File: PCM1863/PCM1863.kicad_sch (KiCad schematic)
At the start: 34 parts, among them IC1 SN74AUC1G126DCKR, IC2 NCP163ASN330T1G, IC3 NCP163ASN330T1G, J1 Conn_01x10_Male, J2 Conn_01x10_Male, J3 Conn_01x10_Male, U1 PCM1863, Y1 ASE-24.000MHZ-ET, Y2 ASE-22.000MHZ-ET

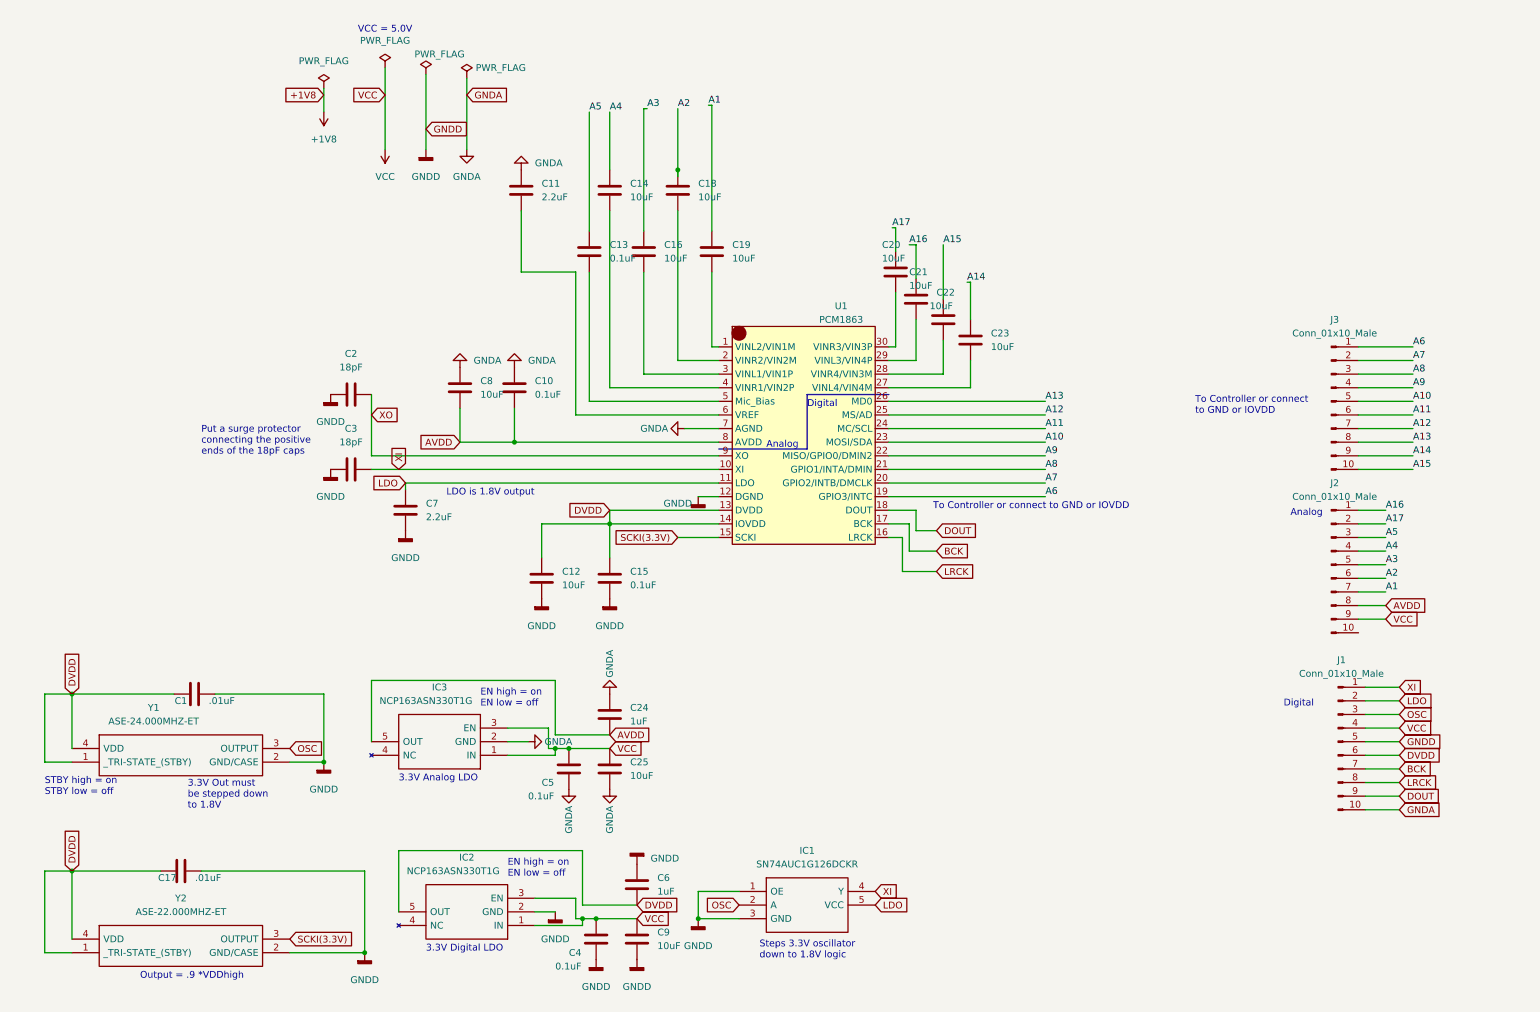
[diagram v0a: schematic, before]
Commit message: 1863 power added and schematic updated
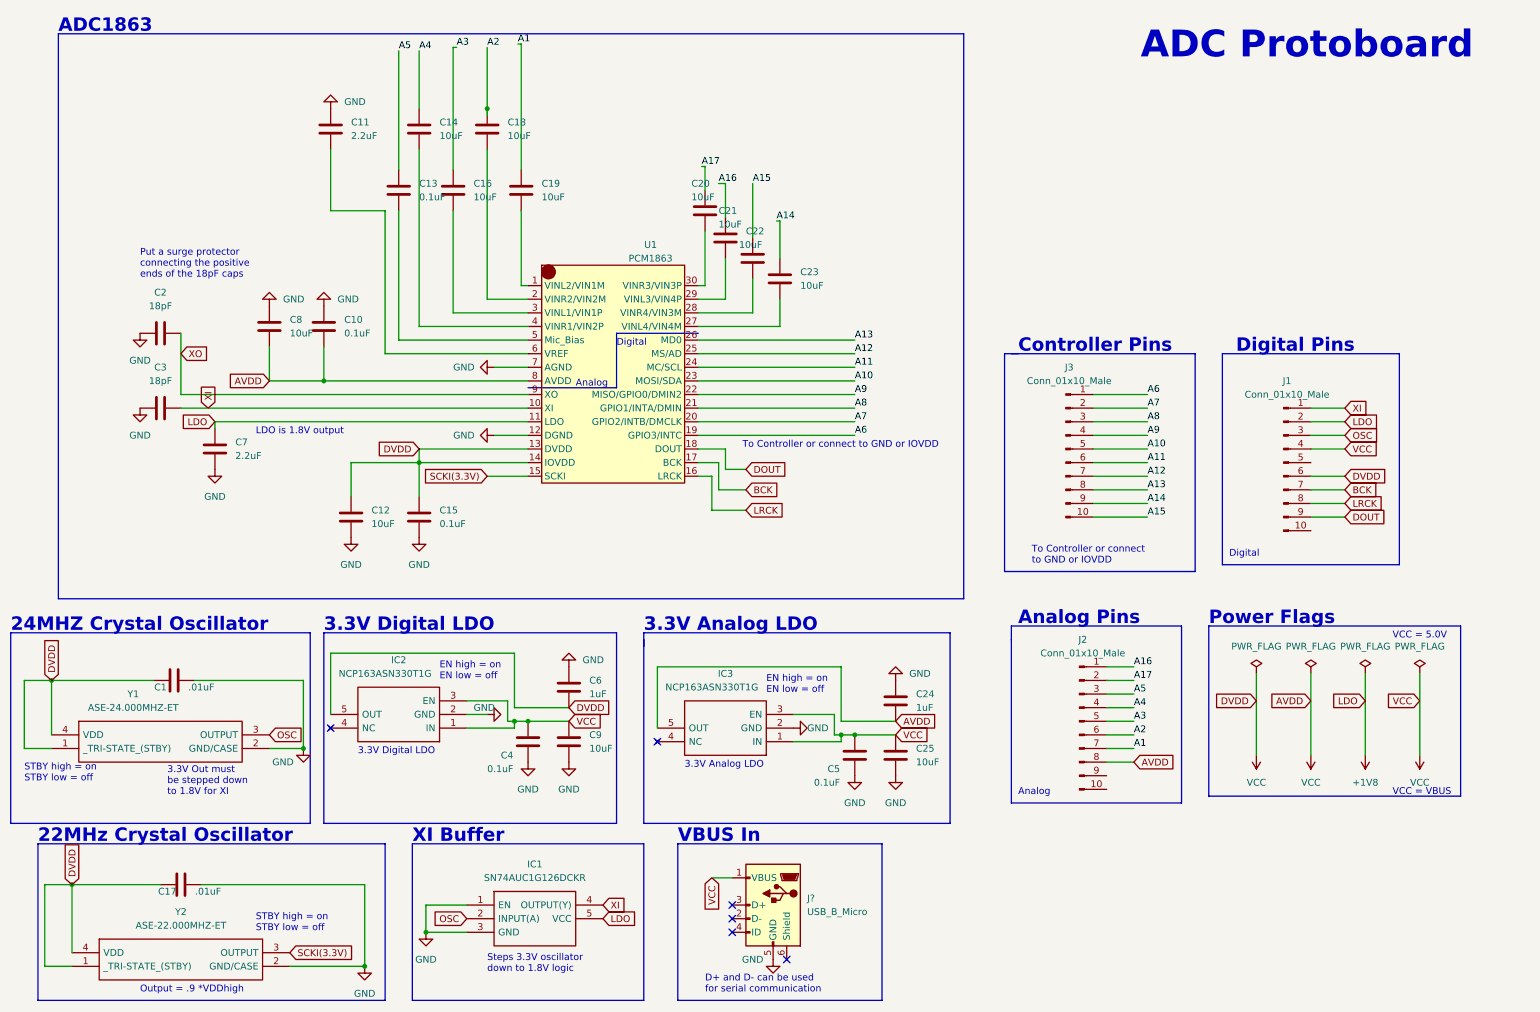
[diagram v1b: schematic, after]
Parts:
- added J?: USB_B_Micro, Connector_USB:USB_Micro-B_Wuerth_629105150521, symbol Connector:USB_B_Micro
- IC1: footprint custom_lib:SOT65P210X110-5N -> SOT65P210X110-5N
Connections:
- net AVDD is gone; now on net VCC: C10.2, C24.2, C8.2, IC3.5 (OUT), J2.8 (Pin_8), U1.8 (AVDD)
- net DVDD is gone; now on net VCC: C1.1, C12.1, C15.1, C17.1, C6.2, IC2.5 (OUT), J1.6 (Pin_6), U1.13 (DVDD), U1.14 (IOVDD), Y1.1 (_TRI-STATE_(STBY)), Y1.4 (VDD), Y2.1 (_TRI-STATE_(STBY)), Y2.4 (VDD)
- net LDO is gone; now on net +1V8: C7.1, IC1.5 (VCC), J1.2 (Pin_2), U1.11 (LDO)
- net VCC: now also J?.1 (VBUS); no longer J2.9 (Pin_9)
- net GNDA renamed GND
- net GND: now also C1.2, C12.2, C15.2, C17.2, C2.1, C3.1, C4.2, C6.1, C7.2, C9.2, IC1.1 (EN), IC1.3 (GND), IC2.2 (GND), U1.12 (DGND), Y1.2 (GND/CASE), Y2.2 (GND/CASE), J?.5 (GND); no longer J1.10 (Pin_10)
- removed net GNDD: C1.2, C12.2, C15.2, C17.2, C2.1, C3.1, C4.2, C6.1, C7.2, C9.2, IC1.1 (OE), IC1.3 (GND), IC2.2 (GND), J1.5 (Pin_5), U1.12 (DGND), Y1.2 (GND/CASE), Y2.2 (GND/CASE)
- no-connect marks 0 -> 6
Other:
- note added: "22MHz Crystal Oscillator"
- note added: "24MHZ Crystal Oscillator"
- note added: "3.3V Out must be stepped down to 1.8V for XI"
- note added: "ADC Protoboard"
- note added: "ADC1863"
- note added: "Analog Pins"
- note added: "Controller Pins"
- note added: "D+ and D- can be used for serial communication"
- note added: "Digital Pins"
- note added: "Power Flags"
- note added: "VBUS In"
- note added: "VCC = VBUS"
- note added: "XI Buffer"
- note removed: "3.3V Out must be stepped down to 1.8V"
- company: (none) -> Chameleon Engine 2023
- title: (none) -> ADC Protoboard
- moved on the sheet: C1, C10, C11, C12, C13, C14, C15, C16, C17, C18, C19, C2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

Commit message: PCB placement no trace
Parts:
- added D1, D2, D3: RED1.8, LED_SMD:LED_0603_1608Metric_Pad1.05x0.95mm_HandSolder, symbol Device:LED
- added R1, R2, R3: 2.2k, Resistor_SMD:R_0603_1608Metric_Pad0.98x0.95mm_HandSolder, symbol Device:R
- IC1: footprint SOT65P210X110-5N -> custom_lib:SOT65P210X110-5N
- gave numbers to parts that had none: 1
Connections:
- net +1V8: now also D1.2 (A)
- net GND: now also R1.2, R2.2, R3.2
- net VCC: no longer C1.1, C10.2, C12.1, C15.1, C17.1, C24.2, C6.2, C8.2, IC2.5 (OUT), IC3.5 (OUT), J1.6 (Pin_6), J2.8 (Pin_8), U1.13 (DVDD), U1.14 (IOVDD), U1.8 (AVDD), Y1.1 (_TRI-STATE_(STBY)), Y1.4 (VDD), Y2.1 (_TRI-STATE_(STBY)), Y2.4 (VDD)
- new net: D3.1 (K), R3.1
- new net: D1.1 (K), R1.1
- new net: D2.1 (K), R2.1
- new net +3.3VA: C10.2, C24.2, C8.2, D3.2 (A), IC3.5 (OUT), J2.8 (Pin_8), U1.8 (AVDD)
- new net +3V3: C1.1, C12.1, C15.1, C17.1, C6.2, D2.2 (A), IC2.5 (OUT), J1.6 (Pin_6), U1.13 (DVDD), U1.14 (IOVDD), Y1.1 (_TRI-STATE_(STBY)), Y1.4 (VDD), Y2.1 (_TRI-STATE_(STBY)), Y2.4 (VDD)

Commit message: adc v3 complete
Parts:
- added D4: RED1.8, LED_SMD:LED_0603_1608Metric_Pad1.05x0.95mm_HandSolder, symbol Device:LED
- added H1, H2, H3, H4: MountingHole_Pad, MountingHole:MountingHole_2.2mm_M2_Pad, symbol Mechanical:MountingHole_Pad
- added R4: 2.2k, Resistor_SMD:R_0603_1608Metric_Pad0.98x0.95mm_HandSolder, symbol Device:R
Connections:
- net +1V8: now also J1.5 (Pin_5); no longer J1.2 (Pin_2)
- net +3.3VA: now also J2.10 (Pin_10); no longer J2.8 (Pin_8)
- net +3V3: now also J1.2 (Pin_2); no longer J1.6 (Pin_6)
- net A1: now also J2.8 (Pin_8); no longer J2.7 (Pin_7)
- net A10: now also J3.7 (Pin_7); no longer J3.5 (Pin_5)
- net A11: now also J3.8 (Pin_8); no longer J3.6 (Pin_6)
- net A12: now also J3.9 (Pin_9); no longer J3.7 (Pin_7)
- net A13: now also J3.10 (Pin_10); no longer J3.8 (Pin_8)
- net A14: now also J2.1 (Pin_1); no longer J3.9 (Pin_9)
- net A15: now also J2.2 (Pin_2); no longer J3.10 (Pin_10)
- net A16: now also J2.3 (Pin_3); no longer J2.1 (Pin_1)
- net A17: now also J2.4 (Pin_4); no longer J2.2 (Pin_2)
- net A2: now also J2.9 (Pin_9); no longer J2.6 (Pin_6)
- net A3: now also J2.7 (Pin_7); no longer J2.5 (Pin_5)
- net A4: now also J2.6 (Pin_6); no longer J2.4 (Pin_4)
- net A5: now also J2.5 (Pin_5); no longer J2.3 (Pin_3)
- net A6: now also J3.3 (Pin_3); no longer J3.1 (Pin_1)
- net A7: now also J3.4 (Pin_4); no longer J3.2 (Pin_2)
- net A8: now also J3.5 (Pin_5); no longer J3.3 (Pin_3)
- net A9: now also J3.6 (Pin_6); no longer J3.4 (Pin_4)
- net BCK: now also J3.1 (Pin_1); no longer J1.7 (Pin_7)
- net DOUT: now also J3.2 (Pin_2); no longer J1.9 (Pin_9)
- net GND: now also H1.1, H2.1, H3.1, H4.1, R4.1
- net LRCK: now also J1.10 (Pin_10); no longer J1.8 (Pin_8)
- net VCC: now also J1.1 (Pin_1), D4.2 (A); no longer J1.4 (Pin_4)
- net XI: now also J1.4 (Pin_4); no longer J1.1 (Pin_1)
- new net: D4.1 (K), R4.2
- no-connect marks 6 -> 10
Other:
- note added: "Mounting Holes"

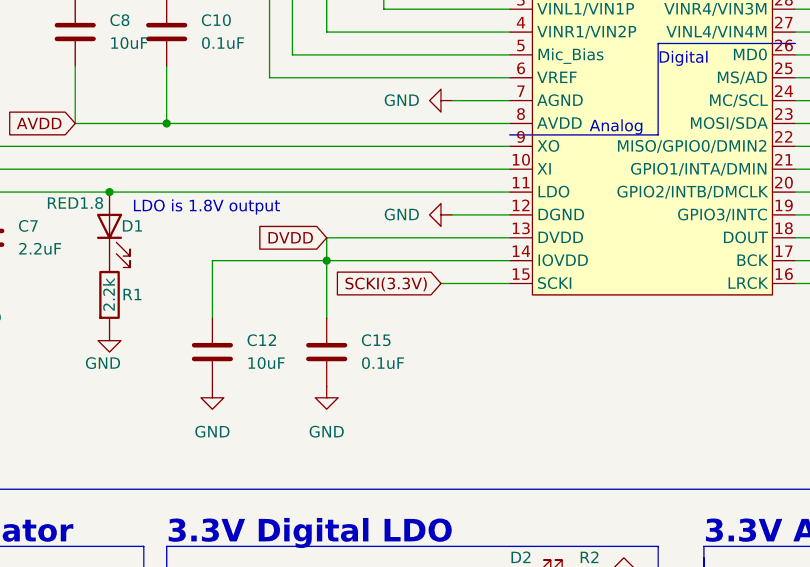
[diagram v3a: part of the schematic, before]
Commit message: fix analog too close to digital
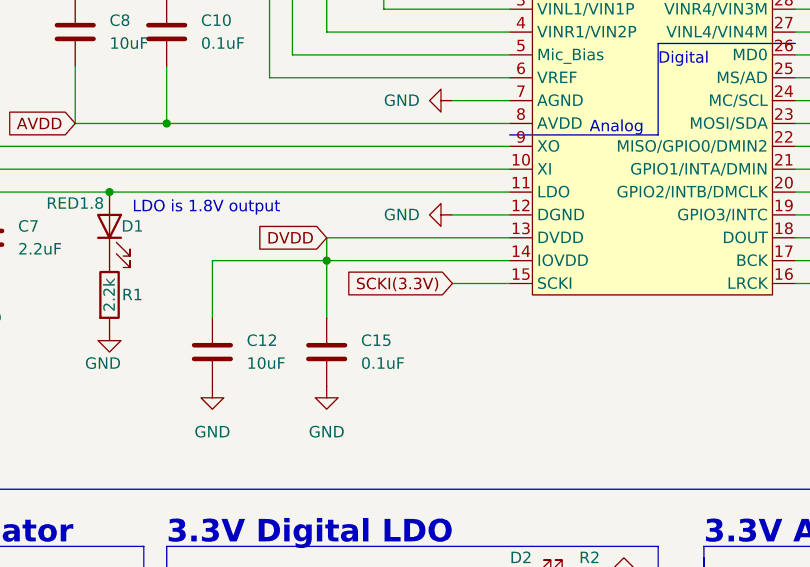
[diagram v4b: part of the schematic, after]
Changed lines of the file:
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@@
     (stroke (width 0) (type default) (color 0 0 0 0))
   )
-  (wire (pts (xy 100.33 99.06) (xy 107.95 99.06))
+  (wire (pts (xy 101.6 99.06) (xy 107.95 99.06))
     (stroke (width 0) (type default) (color 0 0 0 0))
   )
@@
     )
   )
-  (global_label "SCKI(3.3V)" (shape input) (at 100.33 99.06 180) (fields_autoplaced)
+  (global_label "SCKI(3.3V)" (shape input) (at 101.6 99.06 180) (fields_autoplaced)
     (effects (font (size 1.27 1.27)) (justify right))
-    (property "Intersheet References" "${INTERSHEET_REFS}" (id 0) (at 87.7569 98.9806 0)
+    (property "Intersheet References" "${INTERSHEET_REFS}" (id 0) (at 89.0269 98.9806 0)
       (effects (font (size 1.27 1.27)) (justify right) hide)
     )

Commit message: added jumpers
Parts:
- added C26, C27: 10uF-16V, Capacitor_SMD:C_0805_2012Metric_Pad1.18x1.45mm_HandSolder, symbol Device:C
- added C28, C29: 0.1uF-16V, Capacitor_SMD:C_0402_1005Metric_Pad0.74x0.62mm_HandSolder, symbol Device:C
- added IC4: TXB0101DBVT, custom_lib:SOT95P280X145-6N, symbol custom_lib:TXB0101DBVT
- added JP1, JP2, JP3, JP4: Jumper_3_Open, symbol Jumper:Jumper_3_Open
- added JP5, JP7: Jumper_2_Bridged, TestPoint:TestPoint_Bridge_Pitch2.54mm_Drill1.0mm, symbol Jumper:Jumper_2_Bridged
- added JP6: Jumper_2_Open, TestPoint:TestPoint_Bridge_Pitch2.54mm_Drill1.0mm, symbol Jumper:Jumper_2_Open
- added R10, R11, R15, R16, R19, R20, R5, R6: 2.2k, Resistor_SMD:R_0603_1608Metric_Pad0.98x0.95mm_HandSolder, symbol Device:R
- added R12, R13, R17, R18, R21, R22, R7, R8: 100k, Resistor_SMD:R_0402_1005Metric_Pad0.72x0.64mm_HandSolder, symbol Device:R
- added R14, R9: 0, Resistor_SMD:R_0603_1608Metric_Pad0.98x0.95mm_HandSolder, symbol Device:R
- added R23: 4.99k, Resistor_SMD:R_0402_1005Metric_Pad0.72x0.64mm_HandSolder, symbol Device:R
- C10, C15: value 0.1uF -> 0.1uF-16V; footprint Capacitor_SMD:C_0603_1608Metric_Pad1.08x0.95mm_HandSolder -> Capacitor_SMD:C_0402_1005Metric_Pad0.74x0.62mm_HandSolder
- C12, C14: value 10uF -> 10uF-10V
- C13: value 0.1uF -> 0.1uF-50V
- C16: value 10uF -> 0.1uF-16V; footprint Capacitor_SMD:C_0603_1608Metric_Pad1.08x0.95mm_HandSolder -> Capacitor_SMD:C_0402_1005Metric_Pad0.74x0.62mm_HandSolder
- C18, C19, C20, C21, C22, C23: value 10uF -> 10uF-16V; footprint Capacitor_SMD:C_0603_1608Metric_Pad1.08x0.95mm_HandSolder -> Capacitor_SMD:C_0805_2012Metric_Pad1.18x1.45mm_HandSolder
- C2, C3: value 18pF -> 20pF-50V
- C8: value 10uF -> 10uF-10V; footprint Capacitor_SMD:C_0603_1608Metric_Pad1.08x0.95mm_HandSolder -> Capacitor_SMD:C_0805_2012Metric_Pad1.18x1.45mm_HandSolder
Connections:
- net +1V8: now also C14.1, C16.1, C29.2, IC4.1 (VCCA)
- net +3.3VA: now also R9.1; no longer C10.2, C8.2, U1.8 (AVDD)
- net +3V3: now also C28.1, IC4.6 (VCCB), R14.1, R23.1; no longer C12.1, C15.1, U1.13 (DVDD), U1.14 (IOVDD)
- net A1: no longer C19.1
- net A14: no longer C23.1
- net A15: no longer C22.1
- net A16: no longer C21.1
- net A17: no longer C20.1
- net A2: no longer C18.1
- net A3: no longer C16.1
- net A4: no longer C14.1
- net A5: no longer C13.1
- net GND: now also C13.1, C14.2, C16.2, C28.2, C29.1, IC4.2 (GND), JP1.2 (C), JP2.2 (C), JP3.2 (C), JP4.2 (C), JP5.2 (B), JP6.2 (B), R12.1, R13.2, R17.1, R18.2, R21.1, R22.2, R7.1, R8.2
- net XI: now also JP6.1 (A)
- net XO: now also JP7.1 (A)
- net 3L: now reaches C21.2, U1.29 (VINL3/VIN4P)
- net 4L: now reaches C23.2, U1.27 (VINL4/VIN4M)
- net MICBIAS: now reaches C13.2, U1.5 (Mic_Bias)
- net MICBIAS: now also R10.1, R11.1, R15.1, R16.1, R19.1, R20.1, R5.1, R6.1
- net 1L: now reaches U1.3 (VINL1/VIN1P)
- net 1L: now also C19.2; no longer C16.2
- net 2L: now reaches U1.1 (VINL2/VIN1M)
- net 2L: now also C27.2; no longer C19.2
- net 1R: now reaches C18.2
- net 1R: now also U1.4 (VINR1/VIN2P); no longer U1.2 (VINR2/VIN2M)
- net 4R: now reaches C22.2, U1.28 (VINR4/VIN3M)
- net 3R: now reaches C20.2, U1.30 (VINR3/VIN3P)
- new net: IC4.5 (OE), JP5.1 (A), R23.2
- new net: IC4.3 (A), JP7.2 (B)
- new net: C12.1, C15.1, R14.2, U1.13 (DVDD), U1.14 (IOVDD)
- new net: C10.2, C8.2, R9.2, U1.8 (AVDD)
- new net 2R: C26.2, U1.2 (VINR2/VIN2M)
- new net VINL1: C19.1, JP1.3 (B), R5.2, R7.2
- new net VINL2: C27.1, JP2.3 (B), R10.2, R12.2
- new net VINL3: C21.1, JP3.3 (B), R15.2, R17.2
- new net VINL4: C23.1, JP4.3 (B), R19.2, R21.2
- new net VINR1: C18.1, JP1.1 (A), R6.2, R8.1
- new net VINR2: C26.1, JP2.1 (A), R11.2, R13.1
- new net VINR3: C20.1, JP3.1 (A), R16.2, R18.1
- new net VINR4: C22.1, JP4.1 (A), R20.2, R22.1
- new net XO_BUFF: IC4.4 (B)
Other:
- note added: "Put a surge protector connecting the positive ends of the 20pF caps"
- note added: "VIN LR(1-4)"
- note added: "XO Buffer"
- note removed: "Put a surge protector connecting the positive ends of the 18pF caps"
- moved on the sheet: C11, C12, C13, C15, C20, D1, D4, IC1, J4, R1, R4
